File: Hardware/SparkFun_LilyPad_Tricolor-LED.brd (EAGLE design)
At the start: 20 x 20 mm, 17 parts

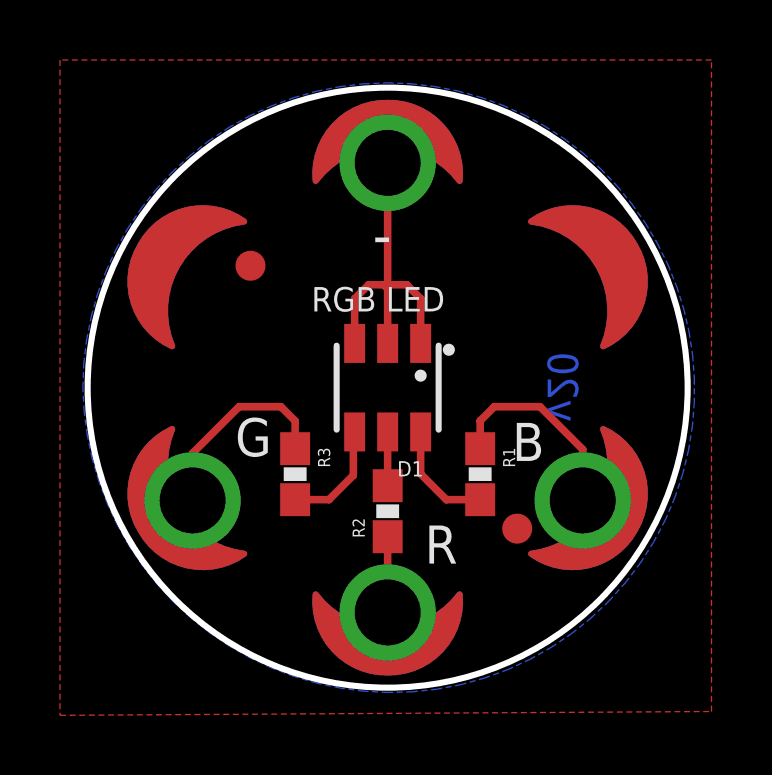
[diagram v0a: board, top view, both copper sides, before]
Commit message: Re-ordered pins, added silk
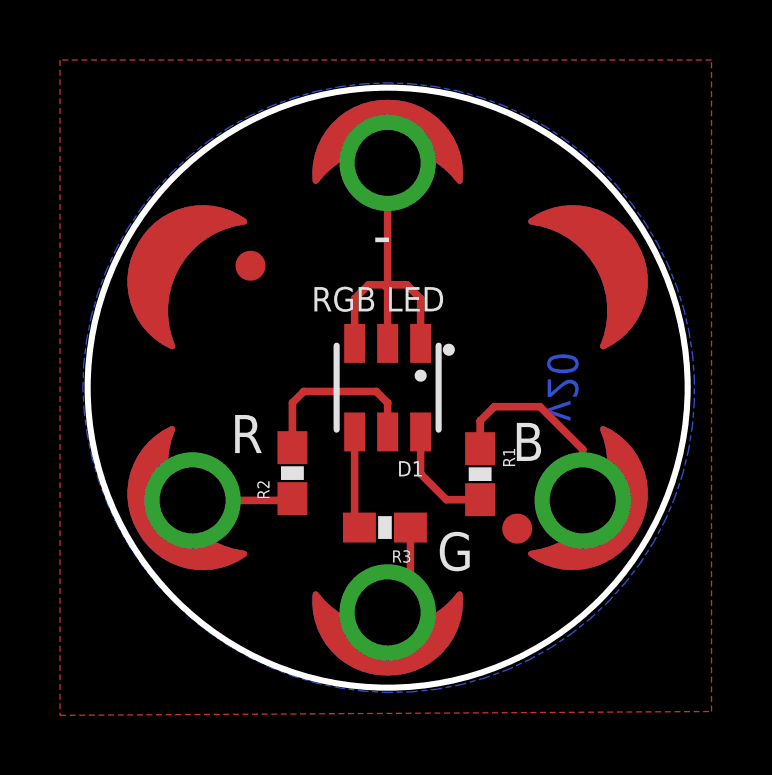
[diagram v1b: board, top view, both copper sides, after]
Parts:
- moved GRN 7.50 mm to (0.00, -7.49), turned to 0 degrees
- moved RED 7.50 mm to (-6.50, -3.76), turned to 300 degrees
- moved R3 3.48 mm to (-0.09, -4.66), turned to 180 degrees
- moved R2 3.42 mm to (-3.17, -2.85)
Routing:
- net RED: track 1.79 -> 5.95 mm
- net N$3: track 6.76 -> 3.14 mm
- net N$2: track 2.52 -> 3.35 mm
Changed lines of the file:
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@@
 <layer number="39" name="tKeepout" color="4" fill="11" visible="no" active="yes"/>
 <layer number="40" name="bKeepout" color="1" fill="11" visible="no" active="yes"/>
-<layer number="41" name="tRestrict" color="4" fill="10" visible="yes" active="yes"/>
+<layer number="41" name="tRestrict" color="4" fill="10" visible="no" active="yes"/>
 <layer number="42" name="bRestrict" color="1" fill="10" visible="no" active="yes"/>
 <layer number="43" name="vRestrict" color="2" fill="10" visible="no" active="yes"/>
@@
 <circle x="0" y="0" radius="5.8309" width="0.0508" layer="47"/>
 <circle x="0" y="0" radius="4.5" width="0.0508" layer="47"/>
-<text x="1.239" y="-5.864" size="1.27" layer="21" font="vector" ratio="15">R</text>
+<text x="-5.238" y="-2.181" size="1.27" layer="21" font="vector" ratio="15">R</text>
 <text x="4.15" y="-2.444" size="1.27" layer="21" font="vector" ratio="15">B</text>
-<text x="-5.082" y="-2.287" size="1.27" layer="21" font="vector" ratio="15">G</text>
+<text x="1.649" y="-6.097" size="1.27" layer="21" font="vector" ratio="15">G</text>
 <text x="-0.5" y="4.392" size="1.4224" layer="21" ratio="15">-</text>
 <polygon width="0.2032" layer="29">
@@
 <text x="-2.667" y="-3.048" size="0.8128" layer="22" font="vector" ratio="15" rot="MR180">RGB LED</text>
 <text x="4.658" y="-3.206" size="1.27" layer="22" font="vector" ratio="15" rot="MR0">B</text>
-<text x="-1.174" y="-5.864" size="1.27" layer="22" font="vector" ratio="15" rot="MR0">R</text>
-<text x="-3.812" y="-3.176" size="1.27" layer="22" font="vector" ratio="15" rot="MR0">G</text>
+<text x="-3.841" y="-3.197" size="1.27" layer="22" font="vector" ratio="15" rot="MR0">R</text>
+<text x="-1.272" y="-6.097" size="1.27" layer="22" font="vector" ratio="15" rot="MR0">G</text>
 </plain>
 <attributes>
@@
 <attribute name="VALUE" value="20" x="3.084" y="-2.884" size="1.778" layer="27" rot="R270" display="off"/>
 </element>
-<element name="R2" library="SparkFun-Resistors" package="0603-RES" value="82" x="0" y="-4.119" rot="R90">
-<attribute name="PROD_ID" value="RES-12311" x="0" y="-4.119" size="1.778" layer="27" rot="R90" display="off"/>
-<attribute name="VALUE" value="82" x="0" y="-4.119" size="1.778" layer="27" rot="R90" display="off"/>
+<element name="R2" library="SparkFun-Resistors" package="0603-RES" value="82" x="-3.175" y="-2.849" rot="R90">
+<attribute name="PROD_ID" value="RES-12311" x="-3.175" y="-2.849" size="1.778" layer="27" rot="R90" display="off"/>
+<attribute name="VALUE" value="82" x="-3.175" y="-2.849" size="1.778" layer="27" rot="R90" display="off"/>
 </element>
-<element name="R3" library="SparkFun-Resistors" package="0603-RES" value="20" x="-3.084" y="-2.884" rot="R270">
-<attribute name="PROD_ID" value="RES-07862" x="-3.084" y="-2.884" size="1.778" layer="27" rot="R270" display="off"/>
-<attribute name="VALUE" value="20" x="-3.084" y="-2.884" size="1.778" layer="27" rot="R270" display="off"/>
+<element name="R3" library="SparkFun-Resistors" package="0603-RES" value="20" x="-0.09" y="-4.663" rot="R180">
+<attribute name="PROD_ID" value="RES-07862" x="-0.09" y="-4.663" size="1.778" layer="27" rot="R180" display="off"/>
+<attribute name="VALUE" value="20" x="-0.09" y="-4.663" size="1.778" layer="27" rot="R180" display="off"/>
 </element>
-<element name="GRN" library="LilyPad-Wearables" package="PETAL-SMALL-2SIDE" value="SEWTAP6" x="-6.5024" y="-3.7592" rot="R300"/>
+<element name="GRN" library="LilyPad-Wearables" package="PETAL-SMALL-2SIDE" value="SEWTAP6" x="0" y="-7.493"/>
 <element name="BLU" library="LilyPad-Wearables" package="PETAL-SMALL-2SIDE" value="SEWTAP6" x="6.5024" y="-3.7592" rot="R60"/>
-<element name="RED" library="LilyPad-Wearables" package="PETAL-SMALL-2SIDE" value="SEWTAP6" x="0" y="-7.493"/>
+<element name="RED" library="LilyPad-Wearables" package="PETAL-SMALL-2SIDE" value="SEWTAP6" x="-6.5024" y="-3.7592" rot="R300"/>
 <element name="GND" library="LilyPad-Wearables" package="PETAL-SMALL-2SIDE" value="SEWTAP6" x="0" y="7.493" rot="R180"/>
 <element name="U$2" library="LilyPad-Wearables" package="PETAL-NOHOLE-2SIDE" value="SEWTAP-NOHOLE2" x="6.5024" y="3.7592" rot="R120"/>
@@
 <contactref element="D1" pad="AR"/>
 <contactref element="R2" pad="2"/>
-<wire x1="0" y1="-1.475" x2="0" y2="-3.269" width="0.254" layer="1"/>
+<wire x1="0" y1="-1.475" x2="0" y2="-0.508" width="0.254" layer="1"/>
+<wire x1="0" y1="-0.508" x2="-0.381" y2="-0.127" width="0.254" layer="1"/>
+<wire x1="-0.381" y1="-0.127" x2="-2.794" y2="-0.127" width="0.254" layer="1"/>
+<wire x1="-2.794" y1="-0.127" x2="-3.175" y2="-0.508" width="0.254" layer="1"/>
+<wire x1="-3.175" y1="-1.999" x2="-3.175" y2="-0.508" width="0.254" layer="1"/>
 </signal>
 <signal name="GRN">
 <contactref element="R3" pad="2"/>
 <contactref element="D1" pad="AG"/>
-<wire x1="-3.084" y1="-3.734" x2="-1.956" y2="-3.734" width="0.254" layer="1"/>
-<wire x1="-1.956" y1="-3.734" x2="-1.143" y2="-2.921" width="0.254" layer="1"/>
-<wire x1="-1.143" y1="-2.921" x2="-1.143" y2="-1.518" width="0.254" layer="1"/>
-<wire x1="-1.143" y1="-1.518" x2="-1.1" y2="-1.475" width="0.254" layer="1"/>
+<wire x1="-1.1" y1="-1.475" x2="-1.1" y2="-4.503" width="0.254" layer="1"/>
+<wire x1="-1.1" y1="-4.503" x2="-0.94" y2="-4.663" width="0.254" layer="1"/>
 </signal>
 <signal name="BLU">
@@
 <contactref element="RED" pad="1"/>
 <contactref element="R2" pad="1"/>
-<wire x1="0" y1="-4.969" x2="0" y2="-7.493" width="0.254" layer="1"/>
+<wire x1="-6.5024" y1="-3.7592" x2="-3.2352" y2="-3.7592" width="0.254" layer="1"/>
+<wire x1="-3.2352" y1="-3.7592" x2="-3.175" y2="-3.699" width="0.254" layer="1"/>
 </signal>
 <signal name="N$3">
 <contactref element="GRN" pad="1"/>
 <contactref element="R3" pad="1"/>
-<wire x1="-6.5024" y1="-3.7592" x2="-6.5024" y2="-2.1844" width="0.254" layer="1"/>
-<wire x1="-6.5024" y1="-2.1844" x2="-4.953" y2="-0.635" width="0.254" layer="1"/>
-<wire x1="-3.084" y1="-2.034" x2="-3.084" y2="-1.107" width="0.254" layer="1"/>
-<wire x1="-3.084" y1="-1.107" x2="-3.556" y2="-0.635" width="0.254" layer="1"/>
-<wire x1="-3.556" y1="-0.635" x2="-4.953" y2="-0.635" width="0.254" layer="1"/>
+<wire x1="0.76" y1="-4.663" x2="0.76" y2="-6.733" width="0.254" layer="1"/>
+<wire x1="0.76" y1="-6.733" x2="0" y2="-7.493" width="0.254" layer="1"/>
 </signal>
 <signal name="N$5">
